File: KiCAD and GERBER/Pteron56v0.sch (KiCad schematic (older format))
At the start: 56 parts, among them J1 AudioJack4, J2 AudioJack4, J3 Conn_01x04, SW10 SW_PUSH, SW12 SW_PUSH, SW13 SW_PUSH, SW14 SW_PUSH, SW15 SW_PUSH, SW17 SW_PUSH, SW18 SW_PUSH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

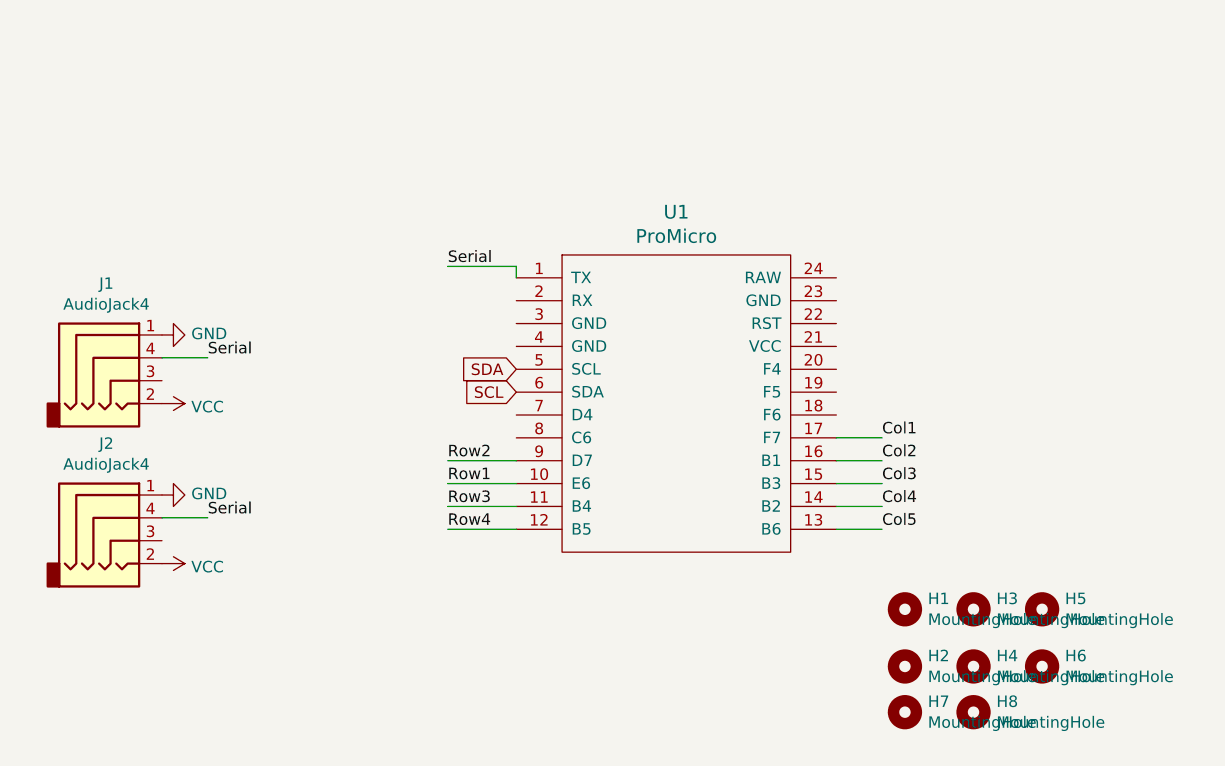
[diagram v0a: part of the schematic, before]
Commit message: add oled, pwm pad, reset switch, moved trrs closer to top, to get simpler casefiles
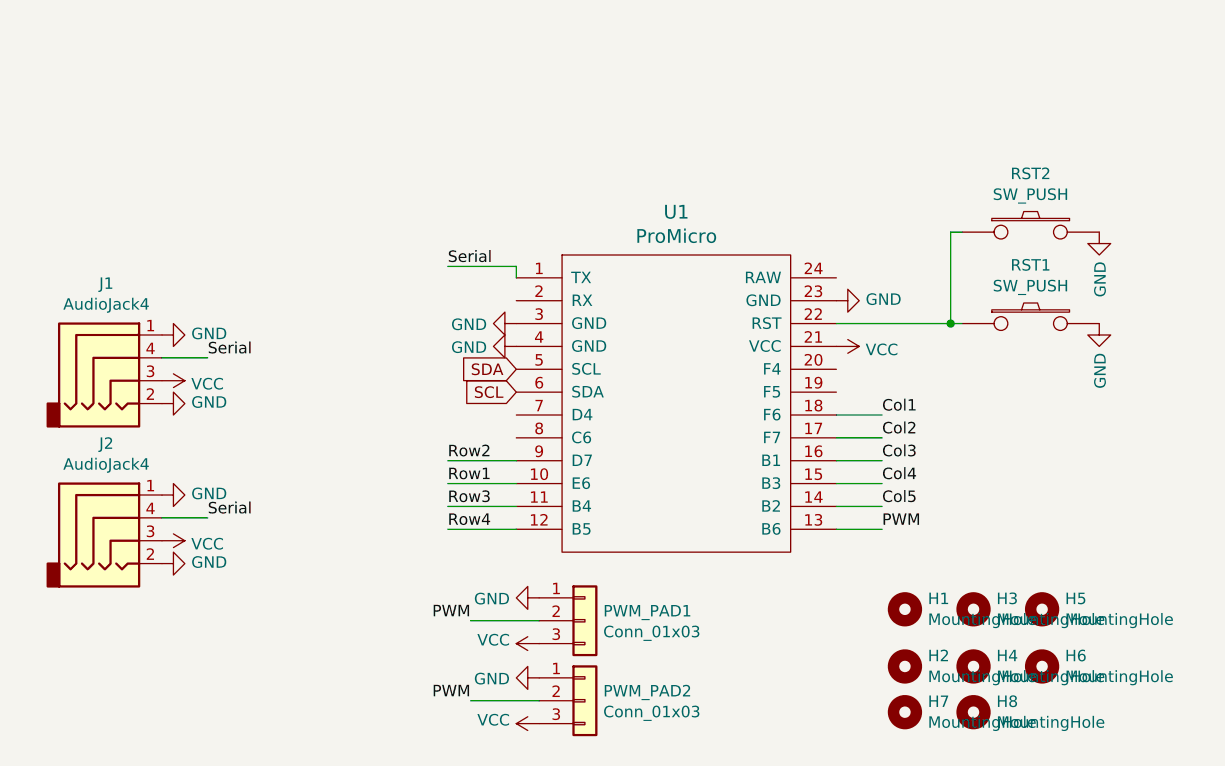
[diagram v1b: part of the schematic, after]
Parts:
- added PWM_PAD1, PWM_PAD2: Conn_01x03, SparkFun-Connectors:1X03_LONGPADS, symbol Connector_Generic:Conn_01x03
- added RST1, RST2: SW_PUSH, acheron_Hardware:smdPushBtn, symbol keyboard_parts:SW_PUSH
- J1, J2: footprint Connector_Audio:Jack_3.5mm_PJ320D_Horizontal -> Keebio-Parts:TRRS-PJ-320A
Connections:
- net Col1: now also U1.18 (F6); no longer U1.17 (F7)
- net Col2: now also U1.17 (F7); no longer U1.16 (B1)
- net Col3: now also U1.16 (B1); no longer U1.15 (B3)
- net Col4: now also U1.15 (B3); no longer U1.14 (B2)
- net Col5: now also U1.14 (B2); no longer U1.13 (B6)
- net GND: now also J1.2, J2.2, U1.23 (GND), U1.3 (GND), U1.4 (GND), PWM_PAD1.1 (Pin_1), PWM_PAD2.1 (Pin_1), RST1.2, RST2.2
- net VCC: now also J1.3, J2.3, U1.21 (VCC), PWM_PAD1.3 (Pin_3), PWM_PAD2.3 (Pin_3); no longer J1.2, J2.2
- net at U1.22 (RST): now also RST1.1, RST2.1
- new net PWM: PWM_PAD1.2 (Pin_2), PWM_PAD2.2 (Pin_2), U1.13 (B6)
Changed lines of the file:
@@
 Text Label 8100 5650 0    50   ~ 0
 Row4
+Text Label 10000 5150 0    50   ~ 0
+Col1
 Text Label 10000 5250 0    50   ~ 0
-Col1
+Col2
 Text Label 10000 5350 0    50   ~ 0
-Col2
+Col3
 Text Label 10000 5450 0    50   ~ 0
-Col3
-Text Label 10000 5550 0    50   ~ 0
 Col4
 Wire Wire Line
@@
 F 0 "J1" H 6607 5225 50  0000 C CNN
 F 1 "AudioJack4" H 6607 5134 50  0000 C CNN
-F 2 "Connector_Audio:Jack_3.5mm_PJ320D_Horizontal" H 6650 4900 50  0001 C CNN
+F 2 "Keebio-Parts:TRRS-PJ-320A" H 6650 4900 50  0001 C CNN
 F 3 "~" H 6650 4900 50  0001 C CNN
 	1    6650 4900
@@
 F 0 "J2" H 6607 5925 50  0000 C CNN
 F 1 "AudioJack4" H 6607 5834 50  0000 C CNN
-F 2 "Connector_Audio:Jack_3.5mm_PJ320D_Horizontal" H 6650 5600 50  0001 C CNN
+F 2 "Keebio-Parts:TRRS-PJ-320A" H 6650 5600 50  0001 C CNN
 F 3 "~" H 6650 5600 50  0001 C CNN
 	1    6650 5600
@@
 L power:VCC #PWR0103
 U 1 1 60852083
-P 6850 5800
-F 0 "#PWR0103" H 6850 5650 50  0001 C CNN
-F 1 "VCC" V 6865 5928 50  0000 L CNN
-F 2 "" H 6850 5800 50  0001 C CNN
-F 3 "" H 6850 5800 50  0001 C CNN
-	1    6850 5800
+P 6850 5700
+F 0 "#PWR0103" H 6850 5550 50  0001 C CNN
+F 1 "VCC" V 6865 5828 50  0000 L CNN
+F 2 "" H 6850 5700 50  0001 C CNN
+F 3 "" H 6850 5700 50  0001 C CNN
+	1    6850 5700
 	0    1    1    0
 $EndComp
@@
 L power:VCC #PWR0104
 U 1 1 608531A6
-P 6850 5100
-F 0 "#PWR0104" H 6850 4950 50  0001 C CNN
-F 1 "VCC" V 6865 5228 50  0000 L CNN
-F 2 "" H 6850 5100 50  0001 C CNN
-F 3 "" H 6850 5100 50  0001 C CNN
-	1    6850 5100
+P 6850 5000
+F 0 "#PWR0104" H 6850 4850 50  0001 C CNN
+F 1 "VCC" V 6865 5128 50  0000 L CNN
+F 2 "" H 6850 5000 50  0001 C CNN
+F 3 "" H 6850 5000 50  0001 C CNN
+	1    6850 5000
 	0    1    1    0
 $EndComp
@@
 Wire Wire Line
 	9800 5450 10000 5450
-Text Label 10000 5650 0    50   ~ 0
+Text Label 10000 5550 0    50   ~ 0
 Col5
 $Comp
@@
 Text GLabel 8400 5050 0    50   Input ~ 0
 SCL
+$Comp
+L power:GND #PWR0109
+U 1 1 607A7400
+P 6850 5100
+F 0 "#PWR0109" H 6850 4850 50  0001 C CNN
+F 1 "GND" V 6855 4972 50  0000 R CNN
+F 2 "" H 6850 5100 50  0001 C CNN
+F 3 "" H 6850 5100 50  0001 C CNN
+	1    6850 5100
+	0    -1   -1   0
+$EndComp
+$Comp
+L power:GND #PWR0110
+U 1 1 607A773D
+P 6850 5800
+F 0 "#PWR0110" H 6850 5550 50  0001 C CNN
+F 1 "GND" V 6855 5672 50  0000 R CNN
+F 2 "" H 6850 5800 50  0001 C CNN
+F 3 "" H 6850 5800 50  0001 C CNN
+	1    6850 5800
+	0    -1   -1   0
+$EndComp
+$Comp
+L keyboard_parts:SW_PUSH RST1
+U 1 1 607B81A2
+P 10650 4750
+F 0 "RST1" H 10650 5005 50  0000 C CNN
+F 1 "SW_PUSH" H 10650 4914 50  0000 C CNN
+F 2 "acheron_Hardware:smdPushBtn" H 10650 4750 60  0001 C CNN
+F 3 "" H 10650 4750 60  0000 C CNN
+	1    10650 4750
+	1    0    0    -1
+$EndComp
+Wire Wire Line
+	9800 4750 10300 4750
+$Comp
+L power:GND #PWR0111
+U 1 1 607BDE0F
+P 8400 4750
+F 0 "#PWR0111" H 8400 4500 50  0001 C CNN
+F 1 "GND" V 8405 4622 50  0000 R CNN
+F 2 "" H 8400 4750 50  0001 C CNN
+F 3 "" H 8400 4750 50  0001 C CNN
+	1    8400 4750
+	0    1    1    0
+$EndComp
+$Comp
+L power:GND #PWR0112
+U 1 1 607BE68F
+P 8400 4850
+F 0 "#PWR0112" H 8400 4600 50  0001 C CNN
+F 1 "GND" V 8405 4722 50  0000 R CNN
+F 2 "" H 8400 4850 50  0001 C CNN
+F 3 "" H 8400 4850 50  0001 C CNN
+	1    8400 4850
+	0    1    1    0
+$EndComp
+$Comp
+L power:GND #PWR0113
+U 1 1 607BE867
+P 9800 4650
+F 0 "#PWR0113" H 9800 4400 50  0001 C CNN
+F 1 "GND" V 9805 4522 50  0000 R CNN
+F 2 "" H 9800 4650 50  0001 C CNN
+F 3 "" H 9800 4650 50  0001 C CNN
+	1    9800 4650
+	0    -1   -1   0
+$EndComp
+$Comp
+L power:GND #PWR0114
+U 1 1 607BF0C8
+P 10950 4750
+F 0 "#PWR0114" H 10950 4500 50  0001 C CNN
+F 1 "GND" V 10955 4622 50  0000 R CNN
+F 2 "" H 10950 4750 50  0001 C CNN
+F 3 "" H 10950 4750 50  0001 C CNN
+	1    10950 4750
+	1    0    0    -1
+$EndComp
+$Comp
+L power:VCC #PWR0115
+U 1 1 607BF74C
+P 9800 4850
+F 0 "#PWR0115" H 9800 4700 50  0001 C CNN
+F 1 "VCC" V 9815 4978 50  0000 L CNN
+F 2 "" H 9800 4850 50  0001 C CNN
+F 3 "" H 9800 4850 50  0001 C CNN
+	1    9800 4850
+	0    1    1    0
+$EndComp
+Wire Wire Line
+	9800 5150 10000 5150
+Text Label 10000 5650 0    50   ~ 0
+PWM
+$Comp
+L Connector_Generic:Conn_01x03 PWM_PAD1
+U 1 1 607D063E
+P 8700 6050
+F 0 "PWM_PAD1" H 8780 6092 50  0000 L CNN
+F 1 "Conn_01x03" H 8780 6001 50  0000 L CNN
+F 2 "SparkFun-Connectors:1X03_LONGPADS" H 8700 6050 50  0001 C CNN
+F 3 "~" H 8700 6050 50  0001 C CNN
+	1    8700 6050
+	1    0    0    -1
+$EndComp
+$Comp
+L power:GND #PWR0116
+U 1 1 607D1939
+P 8500 5950
+F 0 "#PWR0116" H 8500 5700 50  0001 C CNN
+F 1 "GND" V 8505 5822 50  0000 R CNN
+F 2 "" H 8500 5950 50  0001 C CNN
+F 3 "" H 8500 5950 50  0001 C CNN
+	1    8500 5950
+	0    1    1    0
+$EndComp
+$Comp
+L power:VCC #PWR0117
+U 1 1 607D2107
+P 8500 6150
+F 0 "#PWR0117" H 8500 6000 50  0001 C CNN
+F 1 "VCC" V 8515 6278 50  0000 L CNN
+F 2 "" H 8500 6150 50  0001 C CNN
+F 3 "" H 8500 6150 50  0001 C CNN
+	1    8500 6150
+	0    -1   -1   0
+$EndComp
+Text Label 8200 6050 2    50   ~ 0
+PWM
+Wire Wire Line
+	8200 6050 8500 6050
+$Comp
+L keyboard_parts:SW_PUSH RST2
+U 1 1 607E0B2F
+P 10650 4350
+F 0 "RST2" H 10650 4605 50  0000 C CNN
+F 1 "SW_PUSH" H 10650 4514 50  0000 C CNN
+F 2 "acheron_Hardware:smdPushBtn" H 10650 4350 60  0001 C CNN
+F 3 "" H 10650 4350 60  0000 C CNN
+	1    10650 4350
+	1    0    0    -1
+$EndComp
+Wire Wire Line
+	10300 4750 10300 4350
+Wire Wire Line
+	10300 4350 10350 4350
+Connection ~ 10300 4750
+Wire Wire Line
+	10300 4750 10350 4750
+$Comp
+L power:GND #PWR?
+U 1 1 607E5C9B
+P 10950 4350
+F 0 "#PWR?" H 10950 4100 50  0001 C CNN
+F 1 "GND" V 10955 4222 50  0000 R CNN
+F 2 "" H 10950 4350 50  0001 C CNN
+F 3 "" H 10950 4350 50  0001 C CNN
+	1    10950 4350
+	1    0    0    -1
+$EndComp
+$Comp
+L Connector_Generic:Conn_01x03 PWM_PAD2
+U 1 1 607EFD85
+P 8700 6400
+F 0 "PWM_PAD2" H 8780 6442 50  0000 L CNN
+F 1 "Conn_01x03" H 8780 6351 50  0000 L CNN
+F 2 "SparkFun-Connectors:1X03_LONGPADS" H 8700 6400 50  0001 C CNN
+F 3 "~" H 8700 6400 50  0001 C CNN
+	1    8700 6400
+	1    0    0    -1
+$EndComp
+$Comp
+L power:GND #PWR?
+U 1 1 607EFD8B
+P 8500 6300
+F 0 "#PWR?" H 8500 6050 50  0001 C CNN
+F 1 "GND" V 8505 6172 50  0000 R CNN
+F 2 "" H 8500 6300 50  0001 C CNN
+F 3 "" H 8500 6300 50  0001 C CNN
+	1    8500 6300
+	0    1    1    0
+$EndComp
+$Comp
+L power:VCC #PWR?
+U 1 1 607EFD91
+P 8500 6500
+F 0 "#PWR?" H 8500 6350 50  0001 C CNN
+F 1 "VCC" V 8515 6628 50  0000 L CNN
+F 2 "" H 8500 6500 50  0001 C CNN
+F 3 "" H 8500 6500 50  0001 C CNN
+	1    8500 6500
+	0    -1   -1   0
+$EndComp
+Text Label 8200 6400 2    50   ~ 0
+PWM
+Wire Wire Line
+	8200 6400 8500 6400
 $EndSCHEMATC
